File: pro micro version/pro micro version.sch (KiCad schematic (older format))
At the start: 1 part

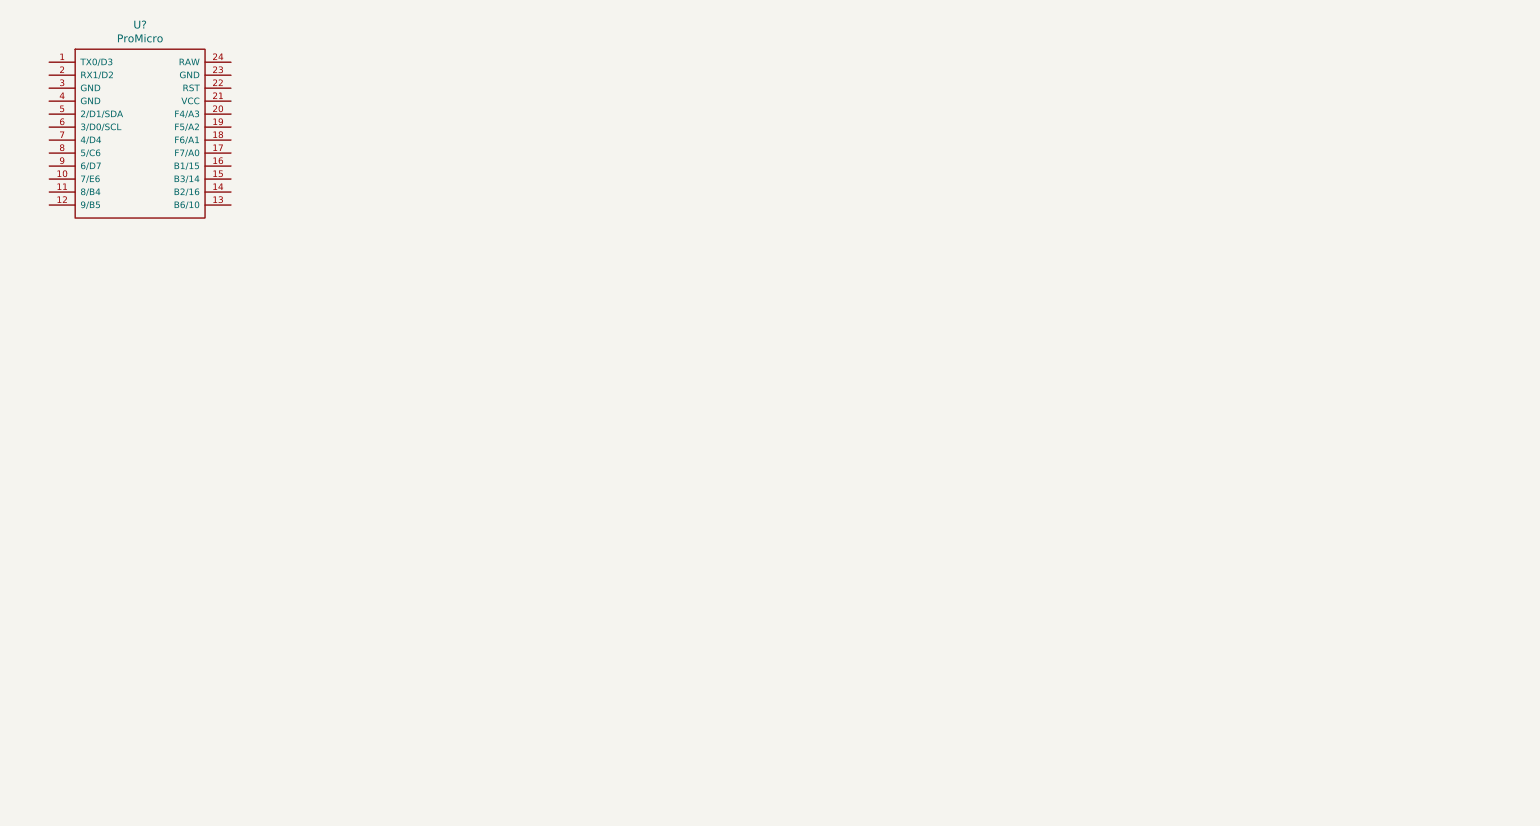
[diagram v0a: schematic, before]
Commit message: left side done plus cleanup of folders and stuff
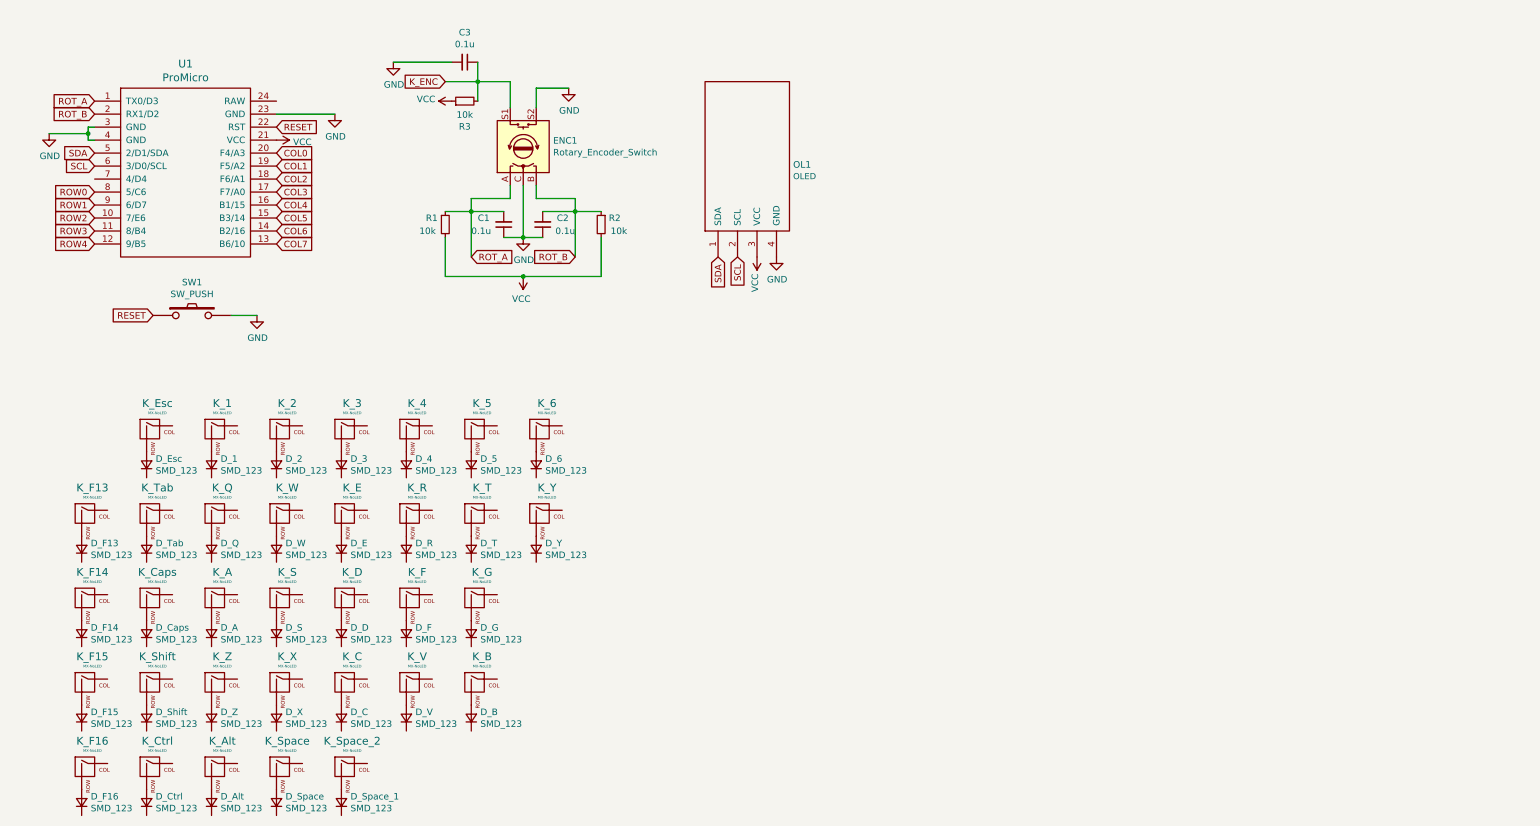
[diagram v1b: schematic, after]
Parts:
- added C1, C2, C3: 0.1u, symbol Device:C_Small
- added D_1, D_2, D_3, D_4, D_5, D_6, D_A, D_Alt, D_B, D_C, D_Caps, D_Ctrl, D_D, D_E, D_Esc, D_F, D_F13, D_F14, D_F15, D_F16, D_G, D_Q, D_R, D_S, D_Shift, D_Space, D_Space_1, D_T, D_Tab, D_V, D_W, D_X, D_Y, D_Z: SMD_123, symbol Device:D_Small
- added ENC1: Rotary_Encoder_Switch, symbol Device:Rotary_Encoder_Switch
- added K_1, K_2, K_3, K_4, K_5, K_6, K_A, K_Alt, K_B, K_C, K_Caps, K_Ctrl, K_D, K_E, K_Esc, K_F, K_F13, K_F14, K_F15, K_F16, K_G, K_Q, K_R, K_S, K_Shift, K_Space, K_Space_2, K_T, K_Tab, K_V, K_W, K_X, K_Y, K_Z: MX-NoLED, symbol MX_Alps_Hybrid:MX-NoLED
- added OL1: OLED, symbol kbd:OLED
- added R1, R2, R3: 10k, symbol Device:R_Small
- added SW1: SW_PUSH, symbol kbd:SW_PUSH
- gave numbers to parts that had none: 1
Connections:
- net ROT_A: now reaches U1.1 (TX0/D3)
- net ROT_A: now also C1.2, ENC1.A, R1.1
- net ROW2: now reaches U1.10 (7/E6)
- net ROW3: now reaches U1.11 (8/B4)
- net ROW4: now reaches U1.12 (9/B5)
- net COL7: now reaches U1.13 (B6/10)
- net COL6: now reaches U1.14 (B2/16)
- net COL5: now reaches U1.15 (B3/14)
- net COL4: now reaches U1.16 (B1/15)
- net COL3: now reaches U1.17 (F7/A0)
- net COL2: now reaches U1.18 (F6/A1)
- net COL1: now reaches U1.19 (F5/A2)
- net ROT_B: now reaches U1.2 (RX1/D2)
- net ROT_B: now also C2.2, ENC1.B, R2.1
- net COL0: now reaches U1.20 (F4/A3)
- net VCC: now reaches U1.21 (VCC)
- net VCC: now also OL1.3 (VCC), R1.2, R2.2, R3.1
- net RESET: now reaches U1.22 (RST)
- net RESET: now also SW1.1
- net GND: now reaches U1.23 (GND)
- net GND: now also U1.3 (GND), U1.4 (GND), C1.1, C2.1, C3.2, ENC1.C, ENC1.S2, OL1.4 (GND), SW1.2
- net SDA: now reaches U1.5 (2/D1/SDA)
- net SDA: now also OL1.1 (SDA)
- net SCL: now reaches U1.6 (3/D0/SCL)
- net SCL: now also OL1.2 (SCL)
- net ROW0: now reaches U1.8 (5/C6)
- net ROW1: now reaches U1.9 (6/D7)
- new net: D_Esc.2 (A), K_Esc.2 (ROW)
- new net: D_1.2 (A), K_1.2 (ROW)
- new net: D_2.2 (A), K_2.2 (ROW)
- new net: D_3.2 (A), K_3.2 (ROW)
- new net: D_4.2 (A), K_4.2 (ROW)
- new net: D_5.2 (A), K_5.2 (ROW)
- new net: D_6.2 (A), K_6.2 (ROW)
- new net: D_Y.2 (A), K_Y.2 (ROW)
- new net: D_F13.2 (A), K_F13.2 (ROW)
- new net: D_F14.2 (A), K_F14.2 (ROW)
- new net: D_F15.2 (A), K_F15.2 (ROW)
- new net: D_F16.2 (A), K_F16.2 (ROW)
- new net: D_Tab.2 (A), K_Tab.2 (ROW)
- new net: D_Caps.2 (A), K_Caps.2 (ROW)
- new net: D_Shift.2 (A), K_Shift.2 (ROW)
- new net: D_Ctrl.2 (A), K_Ctrl.2 (ROW)
- new net: D_Q.2 (A), K_Q.2 (ROW)
- new net: D_A.2 (A), K_A.2 (ROW)
- new net: D_Z.2 (A), K_Z.2 (ROW)
- new net: D_Alt.2 (A), K_Alt.2 (ROW)
- new net: D_W.2 (A), K_W.2 (ROW)
- new net: D_S.2 (A), K_S.2 (ROW)
- new net: D_X.2 (A), K_X.2 (ROW)
- new net: D_Space.2 (A), K_Space.2 (ROW)
- new net: D_E.2 (A), K_E.2 (ROW)
- new net: D_D.2 (A), K_D.2 (ROW)
- new net: D_C.2 (A), K_C.2 (ROW)
- new net: D_Space_1.2 (A), K_Space_2.2 (ROW)
- new net: D_R.2 (A), K_R.2 (ROW)
- new net: D_F.2 (A), K_F.2 (ROW)
- new net: D_V.2 (A), K_V.2 (ROW)
- new net: D_T.2 (A), K_T.2 (ROW)
- new net: D_G.2 (A), K_G.2 (ROW)
- new net: D_B.2 (A), K_B.2 (ROW)
- new net K_ENC: C3.1, ENC1.S1, R3.2
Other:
- moved on the sheet: U1

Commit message: finished sechma
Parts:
- added C1, C2, C3: 0.1u, symbol Device:C_Small
- added D_Alt, D_Apostrophe, D_BSlash, D_Backspace, D_Colon, D_Ctrl, D_DArrow, D_Enter, D_F17, D_F18, D_Fn, D_H, D_I, D_J, D_K, D_L, D_LArrow, D_LBrace, D_LThan, D_M, D_Minus, D_N, D_Num0, D_Num7, D_Num8, D_Num9, D_O, D_P, D_Plus, D_RArrow, D_RBrace, D_RThan, D_Shift, D_Slash, D_Space_3, D_Space_4, D_U, D_UArrow, D_Win: SMD_123, symbol Device:D_Small
- added ENC1: Rotary_Encoder_Switch, symbol Device:Rotary_Encoder_Switch
- added K_Alt, K_Apostrophe, K_BSlash, K_Backspace, K_Colon, K_Ctrl, K_DArrow, K_Enter, K_F17, K_F18, K_Fn, K_H, K_I, K_J, K_K, K_L, K_LArrow, K_LBrace, K_LThan, K_M, K_Minus, K_N, K_Num0, K_Num7, K_Num8, K_Num9, K_O, K_P, K_Plus, K_RArrow, K_RBrace, K_RThan, K_Shift, K_Slash, K_Space_3, K_Space_4, K_U, K_UArrow, K_Win: MX-NoLED, symbol MX_Alps_Hybrid:MX-NoLED
- added OL1: OLED, symbol kbd:OLED
- added R1, R2, R3: 10k, symbol Device:R_Small
- added SW1: SW_PUSH, symbol kbd:SW_PUSH
- added U1: ProMicro, symbol kbd:ProMicro
- renumbered C1 to C4, C2 to C5, C3 to C6, D_1 to D_Num1, D_2 to D_Num2, D_3 to D_Num3, D_4 to D_Num4, D_5 to D_Num5, D_6 to D_Num6, D_Space_1 to D_Space_2, K_1 to K_Num1, K_2 to K_Num2, K_3 to K_Num3, K_4 to K_Num4, K_5 to K_Num5, K_6 to K_Num6, ENC1 to L_ENC1, OL1 to L_OL1, SW1 to L_SW1, U1 to L_U1, R1 to R4, R2 to R5, R3 to R6
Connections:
- net COL0: now also U1.20 (F4/A3); no longer L_U1.20 (F4/A3)
- net COL1: now also U1.19 (F5/A2); no longer L_U1.19 (F5/A2)
- net COL2: now also U1.18 (F6/A1); no longer L_U1.18 (F6/A1)
- net COL3: now also U1.17 (F7/A0); no longer L_U1.17 (F7/A0)
- net COL4: now also U1.16 (B1/15); no longer L_U1.16 (B1/15)
- net COL5: now also U1.15 (B3/14); no longer L_U1.15 (B3/14)
- net COL6: now also U1.14 (B2/16); no longer L_U1.14 (B2/16)
- net COL7: now also U1.13 (B6/10); no longer L_U1.13 (B6/10)
- net GND: now also C1.1, C2.1, C3.2, ENC1.C, ENC1.S2, OL1.4 (GND), SW1.2, U1.23 (GND), U1.3 (GND), U1.4 (GND)
- net K_ENC: now also C3.1, ENC1.S1, R3.2; no longer C6.1, L_ENC1.S1, R6.2
- net RESET: now also SW1.1, U1.22 (RST); no longer L_SW1.1, L_U1.22 (RST)
- net ROT_A: now also C1.2, ENC1.A, R1.1, U1.1 (TX0/D3); no longer C4.2, L_ENC1.A, L_U1.1 (TX0/D3), R4.1
- net ROT_B: now also C2.2, ENC1.B, R2.1, U1.2 (RX1/D2); no longer C5.2, L_ENC1.B, L_U1.2 (RX1/D2), R5.1
- net ROW0: now also U1.8 (5/C6); no longer L_U1.8 (5/C6)
- net ROW1: now also U1.9 (6/D7); no longer L_U1.9 (6/D7)
- net ROW2: now also U1.10 (7/E6); no longer L_U1.10 (7/E6)
- net ROW3: now also U1.11 (8/B4); no longer L_U1.11 (8/B4)
- net ROW4: now also U1.12 (9/B5); no longer L_U1.12 (9/B5)
- net SCL: now also OL1.2 (SCL), U1.6 (3/D0/SCL); no longer L_U1.6 (3/D0/SCL)
- net SDA: now also OL1.1 (SDA), U1.5 (2/D1/SDA); no longer L_U1.5 (2/D1/SDA)
- net VCC: now also OL1.3 (VCC), R1.2, R2.2, R3.1, U1.21 (VCC)
- net L_COL1: now reaches K_Esc.1 (COL)
- net L_COL1: now also K_Caps.1 (COL), K_Ctrl.1 (COL), K_Shift.1 (COL), K_Tab.1 (COL), L_U1.19 (F5/A2), K_I.1 (COL), K_J.1 (COL), K_M.1 (COL), K_Num8.1 (COL), K_Space_4.1 (COL)
- net L_ROW0: now reaches D_Esc.1 (K)
- net L_ROW0: now also D_Num1.1 (K), D_Num2.1 (K), D_Num3.1 (K), D_Num4.1 (K), D_Num5.1 (K), D_Num6.1 (K), L_U1.8 (5/C6), D_Backspace.1 (K), D_Minus.1 (K), D_Num0.1 (K), D_Num7.1 (K), D_Num8.1 (K), D_Num9.1 (K), D_Plus.1 (K)
- net L_COL2: now reaches K_Num1.1 (COL)
- net L_COL2: now also K_A.1 (COL), K_Alt.1 (COL), K_Q.1 (COL), K_Z.1 (COL), L_U1.18 (F6/A1), K_Alt.1 (COL), K_K.1 (COL), K_LThan.1 (COL), K_Num9.1 (COL), K_O.1 (COL)
- net L_COL3: now reaches K_Num2.1 (COL)
- net L_COL3: now also K_S.1 (COL), K_Space.1 (COL), K_W.1 (COL), K_X.1 (COL), L_U1.17 (F7/A0), K_Fn.1 (COL), K_L.1 (COL), K_Num0.1 (COL), K_P.1 (COL), K_RThan.1 (COL)
- net L_COL4: now reaches K_Num3.1 (COL)
- net L_COL4: now also K_C.1 (COL), K_D.1 (COL), K_E.1 (COL), K_Space_2.1 (COL), L_U1.16 (B1/15), K_Colon.1 (COL), K_Ctrl.1 (COL), K_LBrace.1 (COL), K_Minus.1 (COL), K_Slash.1 (COL)
- net L_COL5: now reaches K_Num4.1 (COL)
- net L_COL5: now also K_F.1 (COL), K_R.1 (COL), K_V.1 (COL), L_U1.15 (B3/14), K_Apostrophe.1 (COL), K_LArrow.1 (COL), K_Plus.1 (COL), K_RBrace.1 (COL), K_Shift.1 (COL)
- net L_COL6: now reaches K_Num5.1 (COL)
- net L_COL6: now also K_B.1 (COL), K_G.1 (COL), K_T.1 (COL), L_U1.14 (B2/16), K_BSlash.1 (COL), K_Backspace.1 (COL), K_DArrow.1 (COL), K_Enter.1 (COL), K_UArrow.1 (COL)
- net L_COL7: now reaches K_Num6.1 (COL)
- net L_COL7: now also K_Y.1 (COL), L_U1.13 (B6/10), K_F17.1 (COL), K_F18.1 (COL), K_RArrow.1 (COL), K_Win.1 (COL)
- net L_COL0: now reaches K_F13.1 (COL)
- net L_COL0: now also K_F14.1 (COL), K_F15.1 (COL), K_F16.1 (COL), L_U1.20 (F4/A3), K_H.1 (COL), K_N.1 (COL), K_Num7.1 (COL), K_Space_3.1 (COL), K_U.1 (COL)
- net L_ROW1: now reaches D_Q.1 (K)
- net L_ROW1: now also D_E.1 (K), D_F13.1 (K), D_R.1 (K), D_T.1 (K), D_Tab.1 (K), D_W.1 (K), D_Y.1 (K), L_U1.9 (6/D7), D_BSlash.1 (K), D_F17.1 (K), D_I.1 (K), D_LBrace.1 (K), D_O.1 (K), D_P.1 (K), D_RBrace.1 (K), D_U.1 (K)
- net L_ROW2: now reaches D_Caps.1 (K)
- net L_ROW2: now also D_A.1 (K), D_D.1 (K), D_F.1 (K), D_F14.1 (K), D_G.1 (K), D_S.1 (K), L_U1.10 (7/E6), D_Apostrophe.1 (K), D_Colon.1 (K), D_Enter.1 (K), D_F18.1 (K), D_H.1 (K), D_J.1 (K), D_K.1 (K), D_L.1 (K)
- net L_ROW3: now reaches D_Shift.1 (K)
- net L_ROW3: now also D_B.1 (K), D_C.1 (K), D_F15.1 (K), D_V.1 (K), D_X.1 (K), D_Z.1 (K), L_U1.11 (8/B4), D_LThan.1 (K), D_M.1 (K), D_N.1 (K), D_RThan.1 (K), D_Shift.1 (K), D_Slash.1 (K), D_UArrow.1 (K), D_Win.1 (K)
- net L_ROW4: now reaches D_F16.1 (K)
- net L_ROW4: now also D_Alt.1 (K), D_Ctrl.1 (K), D_Space.1 (K), D_Space_2.1 (K), L_U1.12 (9/B5), D_Alt.1 (K), D_Ctrl.1 (K), D_DArrow.1 (K), D_Fn.1 (K), D_LArrow.1 (K), D_RArrow.1 (K), D_Space_3.1 (K), D_Space_4.1 (K)
- new net: D_Num7.2 (A), K_Num7.2 (ROW)
- new net: D_U.2 (A), K_U.2 (ROW)
- new net: D_H.2 (A), K_H.2 (ROW)
- new net: D_N.2 (A), K_N.2 (ROW)
- new net: D_Space_3.2 (A), K_Space_3.2 (ROW)
- new net: D_Num8.2 (A), K_Num8.2 (ROW)
- new net: D_I.2 (A), K_I.2 (ROW)
- new net: D_J.2 (A), K_J.2 (ROW)
- new net: D_M.2 (A), K_M.2 (ROW)
- new net: D_Space_4.2 (A), K_Space_4.2 (ROW)
- new net: D_Num9.2 (A), K_Num9.2 (ROW)
- new net: D_O.2 (A), K_O.2 (ROW)
- new net: D_K.2 (A), K_K.2 (ROW)
- new net: D_LThan.2 (A), K_LThan.2 (ROW)
- new net: D_Alt.2 (A), K_Alt.2 (ROW)
- new net: D_Num0.2 (A), K_Num0.2 (ROW)
- new net: D_P.2 (A), K_P.2 (ROW)
- new net: D_L.2 (A), K_L.2 (ROW)
- new net: D_RThan.2 (A), K_RThan.2 (ROW)
- new net: D_Fn.2 (A), K_Fn.2 (ROW)
- new net: D_Minus.2 (A), K_Minus.2 (ROW)
- new net: D_LBrace.2 (A), K_LBrace.2 (ROW)
- new net: D_Colon.2 (A), K_Colon.2 (ROW)
- new net: D_Slash.2 (A), K_Slash.2 (ROW)
- new net: D_Ctrl.2 (A), K_Ctrl.2 (ROW)
- new net: D_Plus.2 (A), K_Plus.2 (ROW)
- new net: D_RBrace.2 (A), K_RBrace.2 (ROW)
- new net: D_Apostrophe.2 (A), K_Apostrophe.2 (ROW)
- new net: D_Shift.2 (A), K_Shift.2 (ROW)
- new net: D_LArrow.2 (A), K_LArrow.2 (ROW)
- new net: D_Backspace.2 (A), K_Backspace.2 (ROW)
- new net: D_BSlash.2 (A), K_BSlash.2 (ROW)
- new net: D_Enter.2 (A), K_Enter.2 (ROW)
- new net: D_UArrow.2 (A), K_UArrow.2 (ROW)
- new net: D_DArrow.2 (A), K_DArrow.2 (ROW)
- new net: D_F17.2 (A), K_F17.2 (ROW)
- new net: D_F18.2 (A), K_F18.2 (ROW)
- new net: D_Win.2 (A), K_Win.2 (ROW)
- new net: D_RArrow.2 (A), K_RArrow.2 (ROW)
- new net L_K_ENC: C6.1, L_ENC1.S1, R6.2
- new net L_RESET: L_SW1.1, L_U1.22 (RST)
- new net L_ROT_A: C4.2, L_ENC1.A, L_U1.1 (TX0/D3), R4.1
- new net L_ROT_B: C5.2, L_ENC1.B, L_U1.2 (RX1/D2), R5.1
- new net L_SCL: L_U1.6 (3/D0/SCL)
- new net L_SDA: L_U1.5 (2/D1/SDA)
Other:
- moved on the sheet: C4, C5, C6, D_A, D_Alt, D_B, D_C, D_Caps, D_Ctrl, D_D, D_E, D_Esc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
